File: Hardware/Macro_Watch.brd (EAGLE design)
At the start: 26.7 x 38.4 mm, 28 parts, among them J1 N/P, M1 MF-LED-0805-RED, M16 MF-LED-0805-RED, M2 MF-LED-0805-RED, M32 MF-LED-0805-RED, M4 MF-LED-0805-RED, M8 MF-LED-0805-RED, SW1 MF-SW-TACT-4.2MM, U1 PIC16F527-I/ML, X1 ABS25-32.768KHZ-T

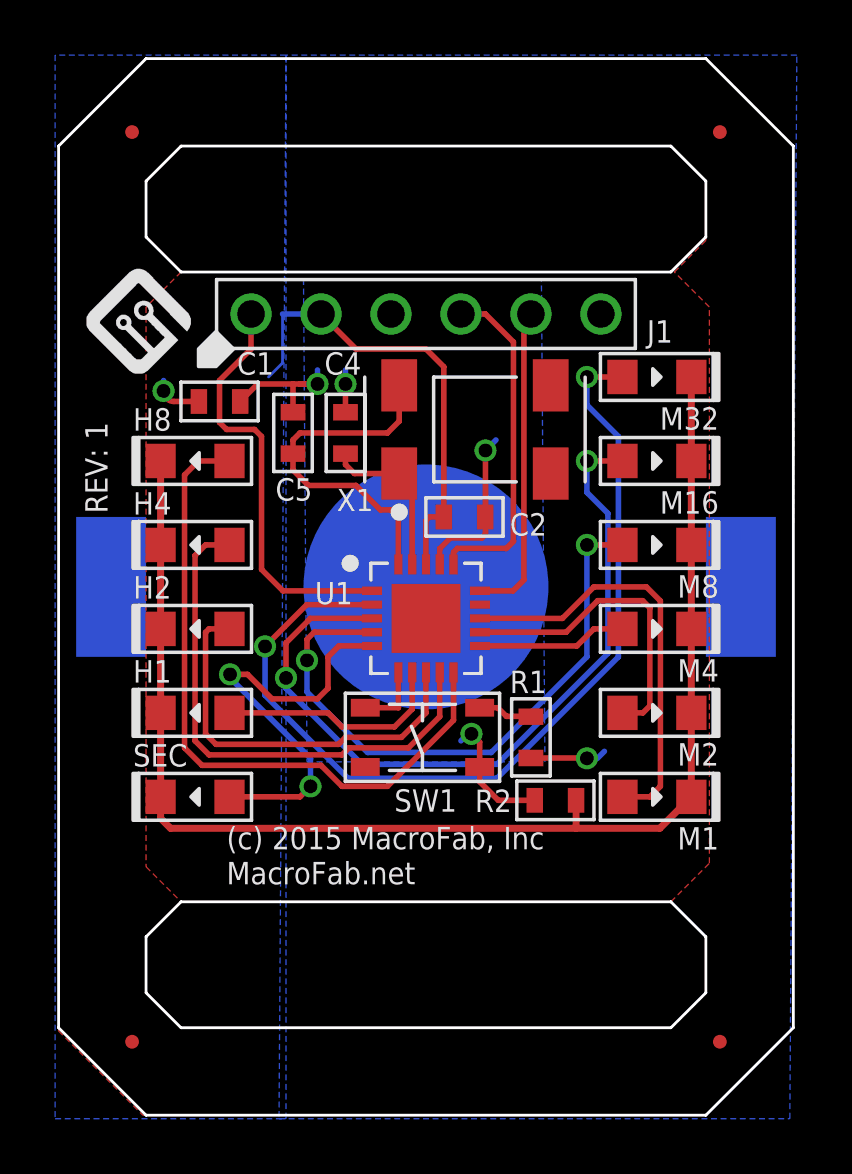
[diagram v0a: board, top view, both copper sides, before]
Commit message: Added working camfiles and tweaked layout.
Added a TP for RA2 pin on MCU. Gerber files have been checked and are
ready for production.
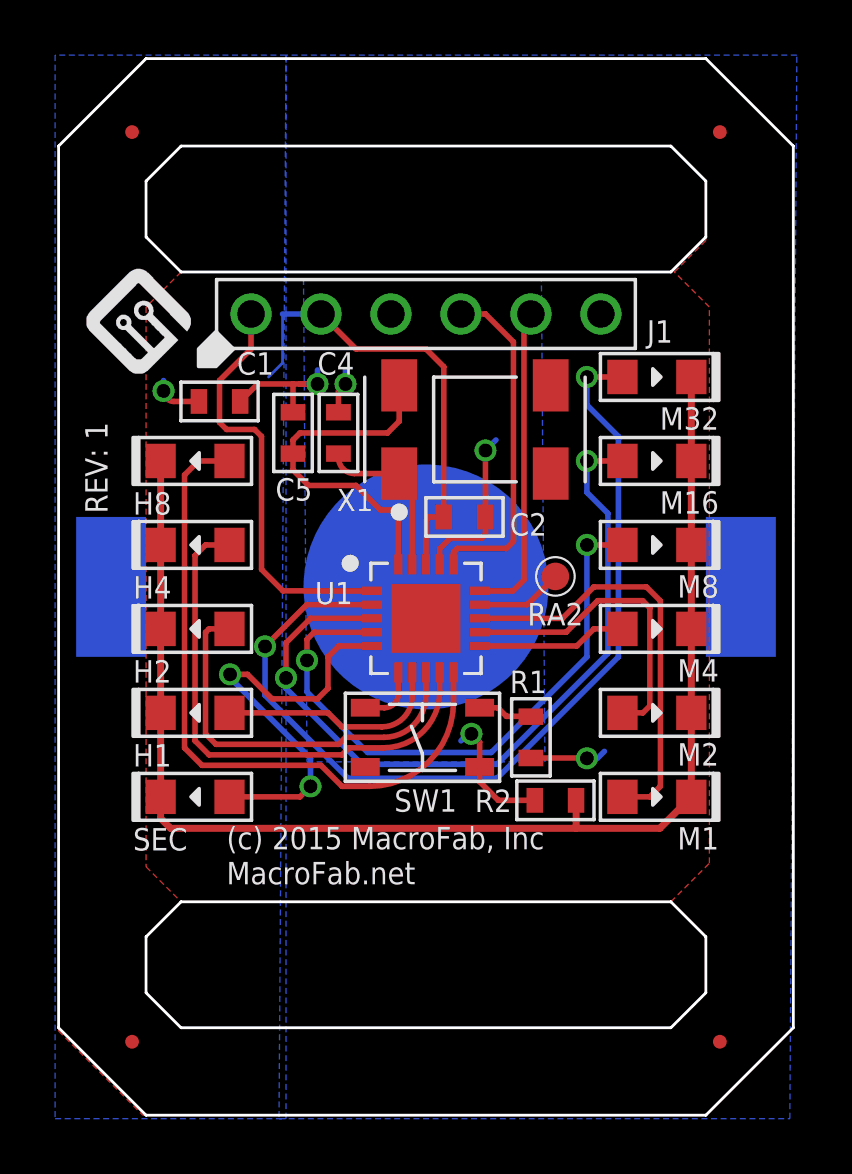
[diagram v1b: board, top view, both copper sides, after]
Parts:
- added RA2: N/P, PP_Connectors:ROUND_TP
- moved C4 0.25 mm to (10.2, 24.8)
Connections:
- net RA2: now also RA2.P$1
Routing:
- net RA2: track 0.00 -> 3.16 mm
- net RB5: track 19.4 -> 18.9 mm
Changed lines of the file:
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@@
 <element name="M16" library="MF_LEDs" package="LED0805" value="MF-LED-0805-RED" x="21.717" y="23.749" rot="R180"/>
 <element name="M32" library="MF_LEDs" package="LED0805" value="MF-LED-0805-RED" x="21.717" y="26.797" rot="R180"/>
-<element name="H1" library="MF_LEDs" package="LED0805" value="MF-LED-0805-GREEN" x="4.953" y="14.605"/>
-<element name="H2" library="MF_LEDs" package="LED0805" value="MF-LED-0805-GREEN" x="4.953" y="17.653"/>
-<element name="H4" library="MF_LEDs" package="LED0805" value="MF-LED-0805-GREEN" x="4.953" y="20.701"/>
-<element name="H8" library="MF_LEDs" package="LED0805" value="MF-LED-0805-GREEN" x="4.953" y="23.749"/>
+<element name="H1" library="MF_LEDs" package="LED0805" value="MF-LED-0805-GREEN" x="4.953" y="14.605" smashed="yes">
+<attribute name="NAME" x="2.703" y="12.657" size="0.8128" layer="25" font="vector" ratio="16"/>
+</element>
+<element name="H2" library="MF_LEDs" package="LED0805" value="MF-LED-0805-GREEN" x="4.953" y="17.653" smashed="yes">
+<attribute name="NAME" x="2.703" y="15.705" size="0.8128" layer="25" font="vector" ratio="16"/>
+</element>
+<element name="H4" library="MF_LEDs" package="LED0805" value="MF-LED-0805-GREEN" x="4.953" y="20.701" smashed="yes">
+<attribute name="NAME" x="2.703" y="18.753" size="0.8128" layer="25" font="vector" ratio="16"/>
+</element>
+<element name="H8" library="MF_LEDs" package="LED0805" value="MF-LED-0805-GREEN" x="4.953" y="23.749" smashed="yes">
+<attribute name="NAME" x="2.703" y="21.801" size="0.8128" layer="25" font="vector" ratio="16"/>
+</element>
 <element name="R2" library="MF_Passives" package="R0603" value="MF-RES-0603-100" x="18.034" y="11.43" smashed="yes">
 <attribute name="TOLERANCE" value="N/A" x="37.084" y="-38.1" size="1.778" layer="27" display="off"/>
@@
 <attribute name="NAME" x="10.097" y="21.923" size="0.8128" layer="25" font="vector" ratio="16"/>
 </element>
-<element name="C4" library="MF_Passives" package="C0603" value="15pF" x="10.414" y="24.765" smashed="yes" rot="R90">
-<attribute name="TOLERANCE" value="N/A" x="56.134" y="66.675" size="1.778" layer="27" rot="R90" display="off"/>
-<attribute name="MFG#" value="N/A" x="56.134" y="66.675" size="1.778" layer="27" rot="R90" display="off"/>
-<attribute name="VOLTAGE" value="N/A" x="56.134" y="66.675" size="1.778" layer="27" rot="R90" display="off"/>
-<attribute name="TEMP_COF" value="N/A" x="56.134" y="66.675" size="1.778" layer="27" rot="R90" display="off"/>
-<attribute name="NAME" x="9.649" y="26.881" size="0.8128" layer="25" font="vector" ratio="16"/>
+<element name="C4" library="MF_Passives" package="C0603" value="15pF" x="10.16" y="24.765" smashed="yes" rot="R90">
+<attribute name="TOLERANCE" value="N/A" x="55.88" y="66.675" size="1.778" layer="27" rot="R90" display="off"/>
+<attribute name="MFG#" value="N/A" x="55.88" y="66.675" size="1.778" layer="27" rot="R90" display="off"/>
+<attribute name="VOLTAGE" value="N/A" x="55.88" y="66.675" size="1.778" layer="27" rot="R90" display="off"/>
+<attribute name="TEMP_COF" value="N/A" x="55.88" y="66.675" size="1.778" layer="27" rot="R90" display="off"/>
+<attribute name="NAME" x="9.395" y="26.881" size="0.8128" layer="25" font="vector" ratio="16"/>
 </element>
 <element name="C5" library="MF_Passives" package="C0603" value="15pF" x="8.509" y="24.765" smashed="yes" rot="R90">
@@
 <attribute name="NAME" x="7.871" y="22.309" size="0.8128" layer="25" font="vector" ratio="16"/>
 </element>
-<element name="SEC" library="MF_LEDs" package="LED0805" value="MF-LED-0805-RED" x="4.953" y="11.557"/>
+<element name="SEC" library="MF_LEDs" package="LED0805" value="MF-LED-0805-RED" x="4.953" y="11.557" smashed="yes">
+<attribute name="NAME" x="2.703" y="9.609" size="0.8128" layer="25" font="vector" ratio="16"/>
+</element>
 <element name="FID1" library="MF_Aesthetics" package="FIDUCIAL_0.5MM" value="FIDUCIAL_0.5MM" x="2.667" y="2.667"/>
 <element name="FID2" library="MF_Aesthetics" package="FIDUCIAL_0.5MM" value="FIDUCIAL_0.5MM" x="2.667" y="35.687"/>
@@
 <element name="FID4" library="MF_Aesthetics" package="FIDUCIAL_0.5MM" value="FIDUCIAL_0.5MM" x="24.003" y="2.667"/>
 <element name="U$1" library="PP_Aesthetics" package="MF_LOGO_SMALL" value="MF_LOGOLOGO_SMALL" x="1.016" y="26.924"/>
+<element name="RA2" library="PP_Connectors" package="ROUND_TP" value="N/P" x="18.034" y="19.558" smashed="yes">
+<attribute name="NAME" x="17.018" y="17.78" size="0.8128" layer="21" font="vector" ratio="16"/>
+</element>
 </elements>
 <signals>
@@
 <wire x1="17.284" y1="11.43" x2="15.961" y2="11.43" width="0.2032" layer="1"/>
 <wire x1="15.961" y1="11.43" x2="15.283" y2="12.108" width="0.2032" layer="1"/>
-<wire x1="10.414" y1="25.515" x2="10.414" y2="26.543" width="0.2032" layer="1"/>
 <via x="10.414" y="26.543" extent="1-16" drill="0.5"/>
 <wire x1="10.414" y1="26.543" x2="10.414" y2="27.051" width="0.2032" layer="16"/>
@@
 <wire x1="7.227" y1="26.543" x2="8.509" y2="26.543" width="0.2032" layer="1"/>
 <wire x1="8.509" y1="26.543" x2="9.398" y2="26.543" width="0.2032" layer="1"/>
+<wire x1="10.16" y1="25.515" x2="10.16" y2="26.289" width="0.2032" layer="1"/>
+<wire x1="10.16" y1="26.289" x2="10.414" y2="26.543" width="0.2032" layer="1"/>
 </signal>
 <signal name="ICSPDAT">
@@
 <wire x1="12.835" y1="23.074" x2="12.363" y2="23.292" width="0.2032" layer="1"/>
 <wire x1="12.363" y1="23.292" x2="10.739153125" y2="23.292" width="0.2032" layer="1"/>
-<wire x1="10.739153125" y1="23.292" x2="10.414" y2="23.617153125" width="0.2032" layer="1"/>
-<wire x1="10.414" y1="23.617153125" x2="10.414" y2="24.015" width="0.2032" layer="1"/>
+<wire x1="10.739153125" y1="23.292" x2="10.16" y2="23.871153125" width="0.2032" layer="1" curve="-90"/>
+<wire x1="10.16" y1="23.871153125" x2="10.16" y2="24.015" width="0.2032" layer="1"/>
 </signal>
 <signal name="RB4">
@@
 <wire x1="4.572" y1="23.241" x2="5.08" y2="23.749" width="0.2032" layer="1"/>
 <wire x1="5.08" y1="23.749" x2="6.203" y2="23.749" width="0.2032" layer="1"/>
-<wire x1="11.938" y1="11.938" x2="10.287" y2="11.938" width="0.2032" layer="1"/>
+<wire x1="14.335" y1="16.074" x2="14.335" y2="14.992534375" width="0.2032" layer="1"/>
+<wire x1="14.335" y1="14.992534375" x2="11.280465625" y2="11.938" width="0.2032" layer="1" curve="-90"/>
+<wire x1="11.280465625" y1="11.938" x2="10.287" y2="11.938" width="0.2032" layer="1"/>
 <wire x1="10.287" y1="11.938" x2="9.525" y2="12.7" width="0.2032" layer="1"/>
 <wire x1="9.525" y1="12.7" x2="5.207" y2="12.7" width="0.2032" layer="1"/>
 <wire x1="5.207" y1="12.7" x2="4.572" y2="13.335" width="0.2032" layer="1"/>
-<wire x1="14.335" y1="16.074" x2="14.335" y2="14.335" width="0.2032" layer="1"/>
-<wire x1="14.335" y1="14.335" x2="11.938" y2="11.938" width="0.2032" layer="1"/>
 </signal>
 <signal name="RB5">
@@
 <wire x1="4.953" y1="20.32" x2="5.334" y2="20.701" width="0.2032" layer="1"/>
 <wire x1="5.334" y1="20.701" x2="6.203" y2="20.701" width="0.2032" layer="1"/>
-<wire x1="13.835" y1="16.074" x2="13.835" y2="14.47" width="0.2032" layer="1"/>
-<wire x1="13.835" y1="14.47" x2="12.7" y2="13.335" width="0.2032" layer="1"/>
-<wire x1="12.7" y1="13.335" x2="10.541" y2="13.335" width="0.2032" layer="1"/>
+<wire x1="13.835" y1="16.074" x2="13.835" y2="15.379321875" width="0.2032" layer="1"/>
+<wire x1="13.835" y1="15.379321875" x2="11.790678125" y2="13.335" width="0.2032" layer="1" curve="-90"/>
+<wire x1="11.790678125" y1="13.335" x2="10.541" y2="13.335" width="0.2032" layer="1"/>
 </signal>
 <signal name="RB6">
@@
 <wire x1="5.334" y1="17.526" x2="5.461" y2="17.653" width="0.2032" layer="1"/>
 <wire x1="5.461" y1="17.653" x2="6.203" y2="17.653" width="0.2032" layer="1"/>
-<wire x1="13.335" y1="16.074" x2="13.335" y2="14.605" width="0.2032" layer="1"/>
-<wire x1="13.335" y1="14.605" x2="12.446" y2="13.716" width="0.2032" layer="1"/>
-<wire x1="12.446" y1="13.716" x2="10.414" y2="13.716" width="0.2032" layer="1"/>
+<wire x1="13.335" y1="16.074" x2="13.335" y2="15.25054375" width="0.2032" layer="1"/>
+<wire x1="13.335" y1="15.25054375" x2="11.80045625" y2="13.716" width="0.2032" layer="1" curve="-90"/>
+<wire x1="11.80045625" y1="13.716" x2="10.414" y2="13.716" width="0.2032" layer="1"/>
 </signal>
 <signal name="RB7">
 <contactref element="U1" pad="P$7"/>
 <contactref element="H1" pad="ANODE"/>
-<wire x1="12.835" y1="16.074" x2="12.835" y2="14.74" width="0.2032" layer="1"/>
+<wire x1="12.835" y1="16.074" x2="12.835" y2="15.1960125" width="0.2032" layer="1"/>
+<wire x1="12.835" y1="15.1960125" x2="11.7359875" y2="14.097" width="0.2032" layer="1" curve="-90"/>
+<wire x1="11.7359875" y1="14.097" x2="10.287" y2="14.097" width="0.2032" layer="1"/>
 <wire x1="10.287" y1="14.097" x2="9.779" y2="14.605" width="0.2032" layer="1"/>
 <wire x1="9.779" y1="14.605" x2="6.203" y2="14.605" width="0.2032" layer="1"/>
-<wire x1="12.835" y1="14.74" x2="12.192" y2="14.097" width="0.2032" layer="1"/>
-<wire x1="12.192" y1="14.097" x2="10.287" y2="14.097" width="0.2032" layer="1"/>
 </signal>
 <signal name="RC1">
@@
 <contactref element="U1" pad="P$6"/>
 <contactref element="SW1" pad="P$1"/>
-<wire x1="12.335" y1="16.074" x2="12.335" y2="14.791" width="0.2032" layer="1"/>
-<wire x1="12.335" y1="14.791" x2="11.133" y2="14.791" width="0.2032" layer="1"/>
+<wire x1="12.335" y1="16.074" x2="12.335" y2="15.302165625" width="0.2032" layer="1"/>
+<wire x1="12.335" y1="15.302165625" x2="11.823834375" y2="14.791" width="0.2032" layer="1" curve="-90"/>
+<wire x1="11.823834375" y1="14.791" x2="11.133" y2="14.791" width="0.2032" layer="1"/>
 </signal>
 <signal name="LED_COM">
@@
 <signal name="RA2">
 <contactref element="U1" pad="P$14"/>
+<contactref element="RA2" pad="P$1"/>
+<wire x1="15.295" y1="18.534" x2="17.01" y2="18.534" width="0.2032" layer="1"/>
+<wire x1="17.01" y1="18.534" x2="18.034" y2="19.558" width="0.2032" layer="1"/>
 </signal>
 <signal name="N$1">
